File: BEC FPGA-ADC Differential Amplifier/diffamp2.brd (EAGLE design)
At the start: 58.1 x 29.2 mm, 23 parts, among them U1 ADA4807-2ARMZRM_8-M, X1 22-23-2031, X3 22-23-2021, X4 22-23-2021

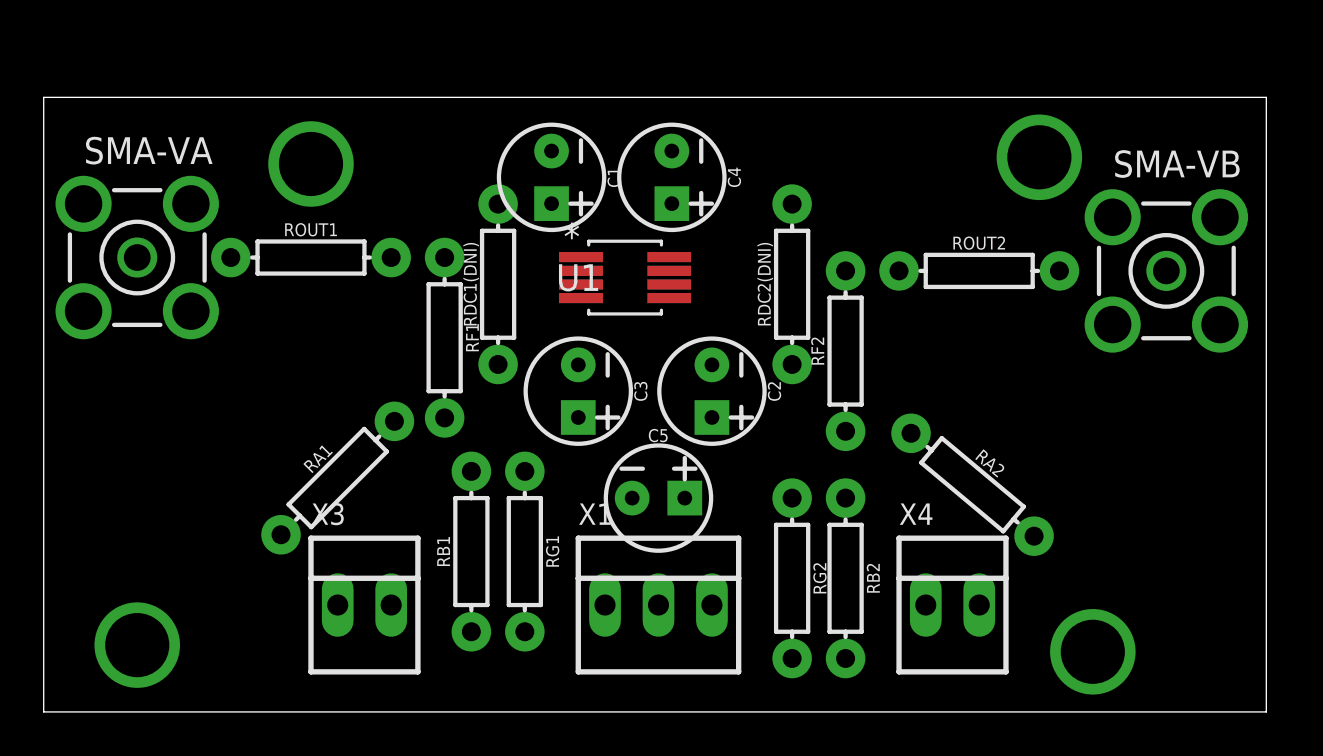
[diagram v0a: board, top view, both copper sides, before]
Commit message: Updated new design, added copper pour for groundplate.
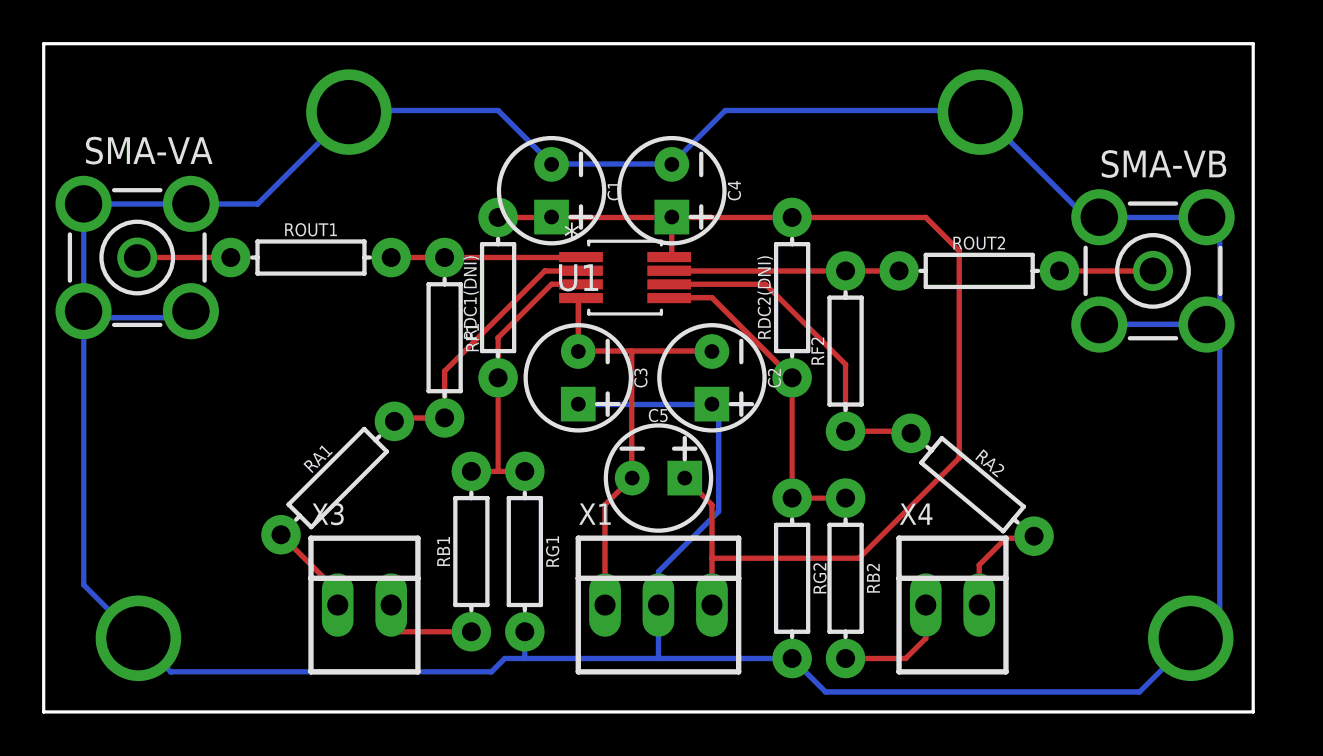
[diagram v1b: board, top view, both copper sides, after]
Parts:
- moved C5 0.95 mm to (29.2, 11.1)
- moved SMA-VB 0.64 mm to (52.7, 21.0)
- moved RDC1(DNI) 0.64 mm to (21.6, 19.7)
- moved RDC2(DNI) 0.64 mm to (35.6, 19.7)
- moved C2 0.63 mm to (31.8, 15.9)
- moved C3 0.63 mm to (25.4, 15.9)
- moved C1 0.63 mm to (24.1, 24.8)
- moved C4 0.63 mm to (29.8, 24.8)
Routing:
- net GND: track 0.00 -> 186.0 mm
- net +5V: track 0.00 -> 54.6 mm
- net -5V: track 0.00 -> 21.5 mm
- net -IN2: track 0.00 -> 16.2 mm
- net +IN2: track 0.00 -> 15.9 mm
- net +IN1: track 0.00 -> 13.8 mm
- net -IN1: track 0.00 -> 13.2 mm
- net VOUT2: track 0.00 -> 10.8 mm
- net VOUT1: track 0.00 -> 9.21 mm
- net DAC-B2: track 0.00 -> 5.79 mm
- net DAC-B1: track 0.00 -> 4.97 mm
- net DAC-A2: track 0.00 -> 4.89 mm
- net VSMA2: track 0.00 -> 4.45 mm
- net VSMA1: track 0.00 -> 4.45 mm
- net DAC-A1: track 0.00 -> 4.23 mm
- added copper zone on layer 16, net GND
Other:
- board size 58.1 x 29.2 mm -> 57.5 x 31.8 mm

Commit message: Updated Silkscreen text, generated gerbers and sent for print.
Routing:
- net DAC-B1: track 4.97 -> 4.29 mm
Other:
- board text added: "2017"
- board text added: "C1"
- board text added: "C2"
- board text added: "C3"
- board text added: "C4"
- board text added: "C5"
- board text added: "Chip ADA4807-2ARMZ"
- board text added: "Designed By"
- board text added: "Diff Amp A"
- board text added: "Diff Amp B"
- board text added: "Differential Amp x2"
- board text added: "Differential Amplifier A"
- board text added: "Differential Amplifier B"
- board text added: "GND"
- board text added: "Inputs"
- board text added: "Matthew Gebert"
- board text added: "RA1"
- board text added: "RA2"
- board text added: "RB1"
- board text added: "RB2"
- board text added: "RDC1 (DNI)"
- board text added: "RDC2 (DNI)"
- board text added: "RF1"
- board text added: "RF2"
- board text added: "RG1"
- board text added: "RG2"
- board text added: "ROUT1"
- board text added: "ROUT2"
- board text added: "Supply"
- board text added: "Va+"
- board text added: "Va-"
- board text added: "Vb+"
- board text added: "Vb-"
- board text added: "Vs+"
- board text added: "Vs-"
- board text added: "github.com/mattgebert/eagleCircuits"
